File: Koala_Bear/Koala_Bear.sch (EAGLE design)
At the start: 21 parts

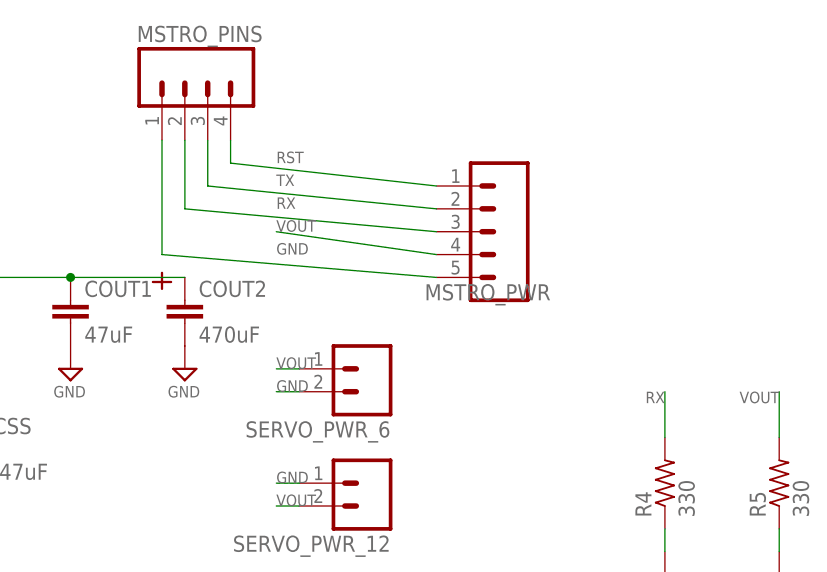
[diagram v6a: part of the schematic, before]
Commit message: Tentative RevB Submission
Changelog:

1. Have adjusted almost all hole positions, though I'm still a bit
worried about clearance. Feedback?
2. Changed LED1 from RX to TX so that it will actually work as intended
(blink when signal is being sent).
3. Made all routing changes suggested by Michael and Dennis (though the
LED trace change actually eliminated a need for one chamfer)

Things I'm worried about:
1. Clearance around the vReg, especially with the big capacitor.
Feedback?
2. Hole clearance
3. We made the decision to remove the holes in the uMaestro block that
would allow screws to be place through the maestro board into the
enclosure, and we also eliminated the holes that would allow a 12-pin
uMaestro to be attached. Do we want to scrap that functionality? The
stand-offs that Kate used in designing the board weren't from the PiE
library, and they aren't even in the standard Eagle library. Some of
them came from SparkFun and others came from a random "servoc" library.
Feedback?

Thanks!
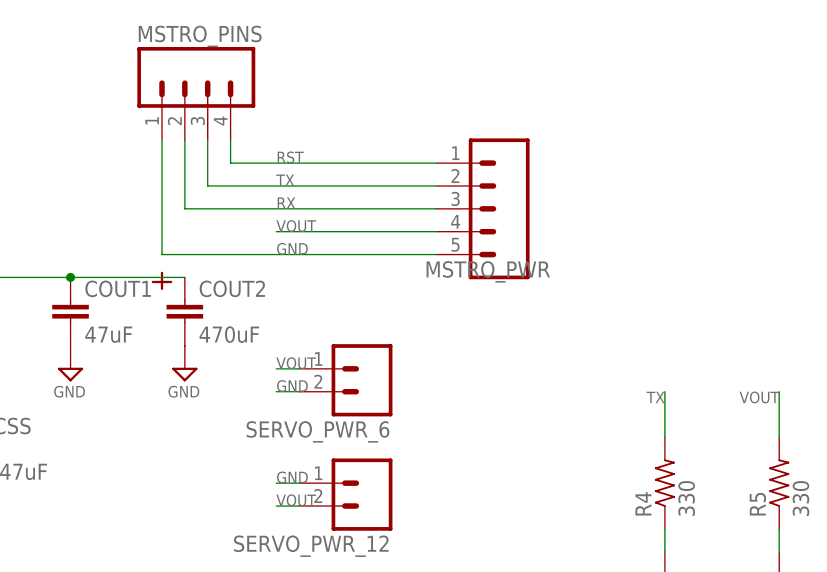
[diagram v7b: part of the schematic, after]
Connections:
- net RX: no longer R4.2
- net TX: now also R4.2
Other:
- moved on the sheet: MSTRO_PWR
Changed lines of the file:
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@@
 </instance>
 <instance part="XT60" gate="G$1" x="-25.4" y="50.8" smashed="yes" rot="R270"/>
-<instance part="MSTRO_PWR" gate="G$1" x="81.28" y="43.18" smashed="yes" rot="R180">
-<attribute name="VALUE" x="86.36" y="55.88" size="1.778" layer="96" font="vector" rot="R180"/>
-<attribute name="NAME" x="86.36" y="37.338" size="1.778" layer="95" font="vector" rot="R180"/>
+<instance part="MSTRO_PWR" gate="G$1" x="81.28" y="45.72" smashed="yes" rot="R180">
+<attribute name="VALUE" x="86.36" y="58.42" size="1.778" layer="96" font="vector" rot="R180"/>
+<attribute name="NAME" x="86.36" y="39.878" size="1.778" layer="95" font="vector" rot="R180"/>
 </instance>
 <instance part="SERVO_PWR_6" gate="G$1" x="66.04" y="27.94" smashed="yes" rot="R180">
@@
 <pinref part="MSTRO_PINS" gate="G$1" pin="1"/>
 <wire x1="43.18" y1="53.34" x2="43.18" y2="40.64" width="0.1524" layer="91"/>
-<wire x1="43.18" y1="40.64" x2="73.66" y2="38.1" width="0.1524" layer="91"/>
+<wire x1="43.18" y1="40.64" x2="73.66" y2="40.64" width="0.1524" layer="91"/>
 </segment>
 <segment>
@@
 <segment>
 <pinref part="MSTRO_PWR" gate="G$1" pin="4"/>
-<wire x1="73.66" y1="40.64" x2="55.88" y2="43.18" width="0.1524" layer="91"/>
+<wire x1="73.66" y1="43.18" x2="55.88" y2="43.18" width="0.1524" layer="91"/>
 <label x="55.88" y="43.18" size="1.27" layer="95" font="vector"/>
 </segment>
@@
 <wire x1="45.72" y1="53.34" x2="45.72" y2="45.72" width="0.1524" layer="91"/>
 <pinref part="MSTRO_PWR" gate="G$1" pin="3"/>
-<wire x1="45.72" y1="45.72" x2="73.66" y2="43.18" width="0.1524" layer="91"/>
+<wire x1="45.72" y1="45.72" x2="73.66" y2="45.72" width="0.1524" layer="91"/>
 <label x="55.88" y="45.72" size="1.27" layer="95"/>
+</segment>
+</net>
+<net name="TX" class="0">
+<segment>
+<pinref part="MSTRO_PINS" gate="G$1" pin="3"/>
+<wire x1="48.26" y1="53.34" x2="48.26" y2="48.26" width="0.1524" layer="91"/>
+<pinref part="MSTRO_PWR" gate="G$1" pin="2"/>
+<wire x1="48.26" y1="48.26" x2="73.66" y2="48.26" width="0.1524" layer="91"/>
+<label x="55.88" y="48.26" size="1.27" layer="95"/>
 </segment>
 <segment>
@@
 </segment>
 </net>
-<net name="TX" class="0">
-<segment>
-<pinref part="MSTRO_PINS" gate="G$1" pin="3"/>
-<wire x1="48.26" y1="53.34" x2="48.26" y2="48.26" width="0.1524" layer="91"/>
-<pinref part="MSTRO_PWR" gate="G$1" pin="2"/>
-<wire x1="48.26" y1="48.26" x2="73.66" y2="45.72" width="0.1524" layer="91"/>
-<label x="55.88" y="48.26" size="1.27" layer="95"/>
-</segment>
-</net>
 <net name="RST" class="0">
 <segment>
@@
 <wire x1="50.8" y1="53.34" x2="50.8" y2="50.8" width="0.1524" layer="91"/>
 <pinref part="MSTRO_PWR" gate="G$1" pin="1"/>
-<wire x1="50.8" y1="50.8" x2="73.66" y2="48.26" width="0.1524" layer="91"/>
+<wire x1="50.8" y1="50.8" x2="73.66" y2="50.8" width="0.1524" layer="91"/>
 <label x="55.88" y="50.8" size="1.27" layer="95"/>
 </segment>

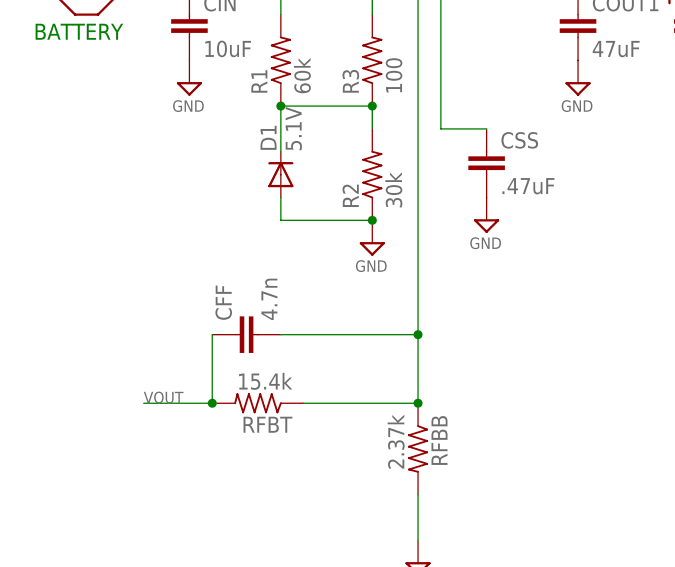
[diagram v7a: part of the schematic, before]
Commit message: Further Review Fixes
1. Duly noted and changed
2. Hoping I removed the correct text
3. Basically, Doug used an oscilloscope today to demonstrate that
current was being sent through the serial line that we didn't have the
LED on. The TX/RX lines should be labeled wrt the Panda, thus why the
signal LED is now on the TX line.
4. Did I do this correctly? Looks like all the vias are now "tented."
5. Okidoke, got it.
6. It didn't have that in the value when it was first constructed, but I
went ahead and added it.
7. Consider them capitalized
8. Consider the value gone
9. I'll run it by Yip on Wednesday at worksession if I can catch him...
10. Glad it's clearer!
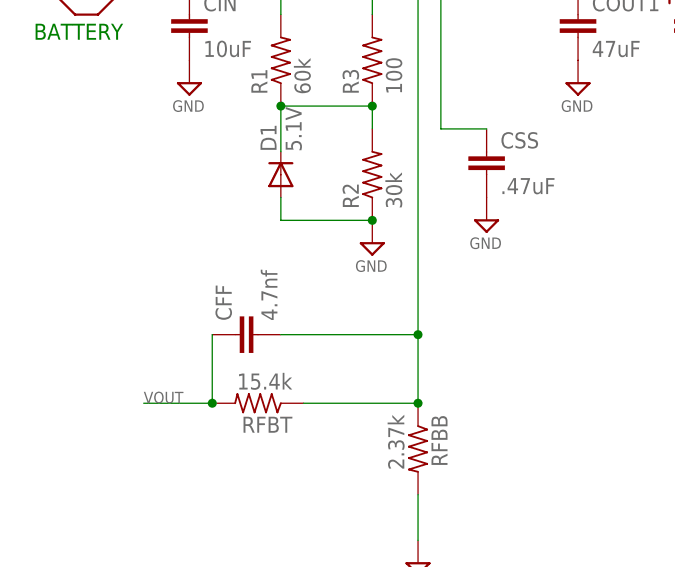
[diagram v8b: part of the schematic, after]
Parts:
- CFF: value 4.7n -> 4.7nf
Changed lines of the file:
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@@
 <part name="RFBT" library="pie" deviceset="R-US_" device="R0603" value="15.4k"/>
 <part name="RFBB" library="pie" deviceset="R-US_" device="R0603" value="2.37k"/>
-<part name="CFF" library="pie" deviceset="CAP" device="0603-CAP" value="4.7n"/>
+<part name="CFF" library="pie" deviceset="CAP" device="0603-CAP" value="4.7nf"/>
 <part name="CSS" library="pie" deviceset="CAP" device="0603-CAP" value=".47uF"/>
 <part name="CIN" library="pie" deviceset="CAP" device="0603-CAP" value="10uF"/>
